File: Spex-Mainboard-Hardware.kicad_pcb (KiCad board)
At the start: 4 copper layers, 100 x 80 mm, 134 parts, among them K1 G5LE_1A4_DC3, K2 G5LE_1A4_DC3, P1 USB_OTG, P10 CONN_01X02, P11 CONN_01X02, P12 CONN_01X02, P13 CONN_01X02, P2 SWD Header, P3 CONN_01X04, P4 CONN_01X04, P5 CONN_01X04, P6 CONN_01X04, P7 CONN_01X02, P8 CONN_01X02, P9 CONN_01X02, Q1 2N7002K, Q101 MOS_N_numbered, Q104 MOS_N_numbered, Q105 Si3407DV, Q106 Q_PNP_BEC, Q2 2N7002K, Q3 BSS215PH6327, Q4 Si5468DC, Q5 Si5468DC, Q6 Si5468DC, SW1 SW_PUSH, U1 MKL04Z32VLC4, U10 LM4030, U105 TPS563200, U108 TPS563200, U11 MCP2551-I/SN, U12 ST1480ABDR, U13 SCHA4B0419, U14 AT45DB641E, U2 NUP2201MR6, U3 MK20DX256VLH7, U4 NUP2201MR6, U5 NUP2201MR6, U6 MMQA6V2T1G, U7 MCP9808T, U8 BME280, U9 LSM9DS1, Y1 Crystal

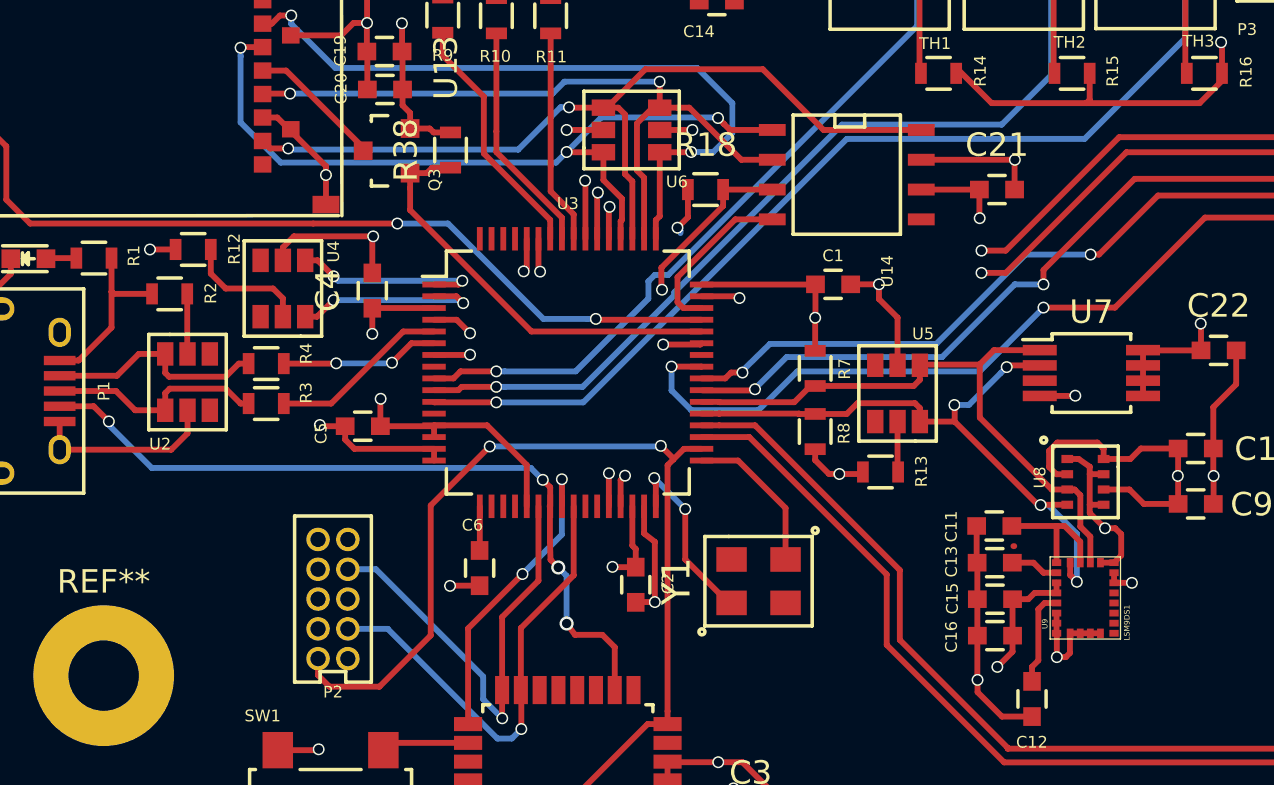
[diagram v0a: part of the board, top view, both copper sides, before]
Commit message: updated BOM, fixed footprints
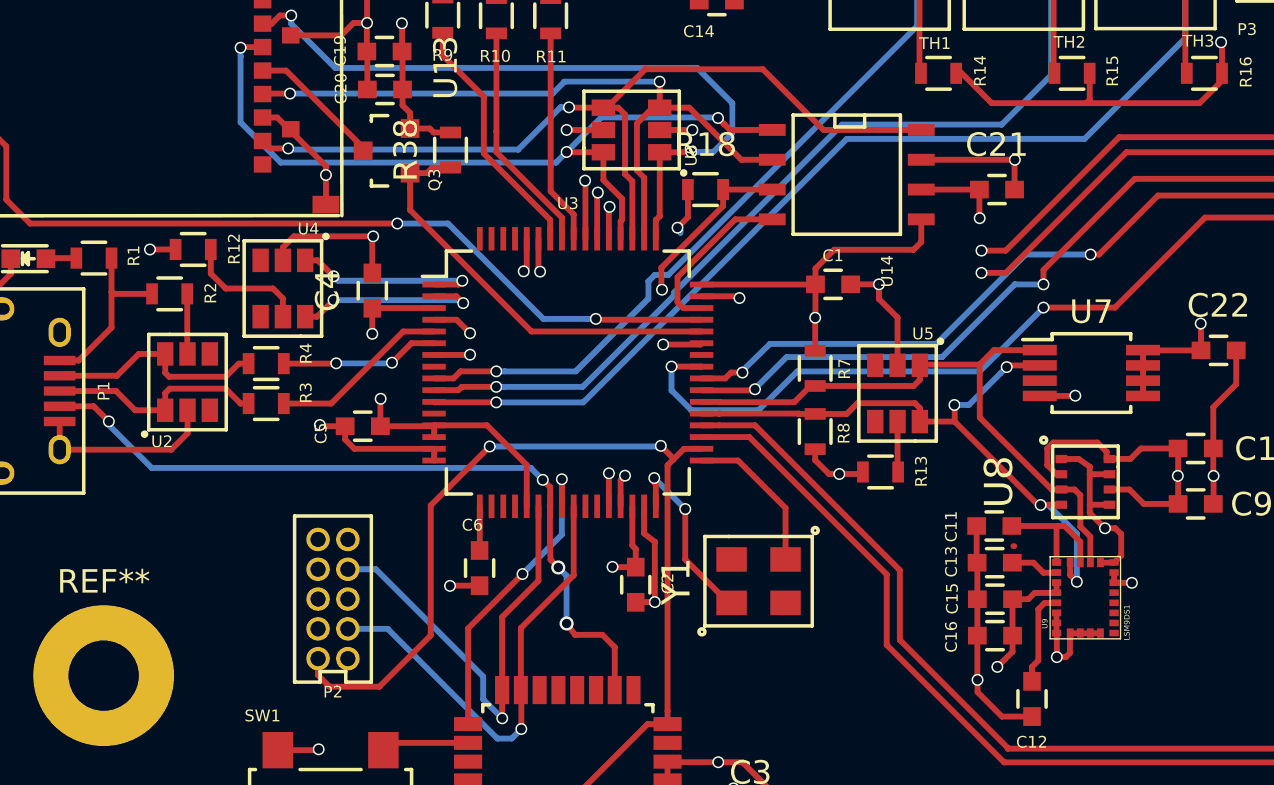
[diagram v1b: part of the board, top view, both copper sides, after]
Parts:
- moved U9 1.95 mm to (131.8, 81.7)
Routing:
- net +3V3: track 131.4 -> 137.6 mm

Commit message: updated PCB
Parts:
- moved REF** 0.19 mm to (90.1, 84.8)
- moved REF** 0.14 mm to (90.0, 125.9)
- moved U13 0.10 mm to (100.0, 65.4)
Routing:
- net (no net): track 2.73 -> 0.07 mm
- net VBatt: track 107.1 -> 107.7 mm
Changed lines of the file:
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@@
     (links 362)
     (no_connects 6)
-    (area 83.744999 50.734999 183.895001 130.885001)
+    (area 79.80956 50.49938 188.775001 131.514133)
     (thickness 1.6)
     (drawings 8)
-    (tracks 1408)
+    (tracks 1406)
     (zones 0)
     (modules 134)
@@
     (0 F.Cu signal)
     (1 In1.Cu power hide)
-    (2 In2.Cu power hide)
+    (2 In2.Cu power)
     (31 B.Cu mixed hide)
     (32 B.Adhes user)
@@
     (user_trace_width 2)
     (trace_clearance 0.15)
-    (zone_clearance 0.1)
+    (zone_clearance 0.508)
     (zone_45_only yes)
     (trace_min 0.2)
@@
     (visible_elements 7FFCFFFF)
     (pcbplotparams
-      (layerselection 0x3ffff_80000007)
+      (layerselection 0x310f0_80000007)
       (usegerberextensions false)
       (excludeedgelayer true)
@@
   )
   (module SPEX_Parts:SCH4B0419 (layer F.Cu)
-    (at 99.8982 65.3796 90)
+    (at 99.99472 65.38976 90)
     (fp_text reference U13 (at 6.2865 4.68884 90) (layer F.SilkS)
       (effects (font (size 1 1) (thickness 0.15)))
@@
   )
   (module Mounting_Holes:MountingHole_3mm_Pad (layer F.Cu)
-    (at 90 126)
+    (at 90.018 125.866)
     (descr "Mounting Hole 3mm")
     (tags "mounting hole 3mm")
@@
   )
   (module Mounting_Holes:MountingHole_3mm_Pad (layer F.Cu)
-    (at 90 85)
+    (at 90.054 84.813)
     (descr "Mounting Hole 3mm")
     (tags "mounting hole 3mm")
@@
     (fp_circle (center 0 0) (end 3 0) (layer Cmts.User) (width 0.15))
     (fp_circle (center 0 0) (end 3.25 0) (layer F.CrtYd) (width 0.05))
-    (pad 1 thru_hole circle (at 0 0) (size 6 6) (drill 3) (layers *.Cu *.Mask F.SilkS))
+    (pad 1 thru_hole circle (at 0.014 0.02) (size 6 6) (drill 3) (layers *.Cu *.Mask F.SilkS))
   )
   (module SPEX_Parts:LGA-8 (layer F.Cu)
@@
   (segment (start 128.766 79.48168) (end 128.8034 79.48168) (width 0.25) (layer F.Cu) (net 0))
   (segment (start 162.5346 78.994) (end 162.56 78.9686) (width 0.25) (layer In2.Cu) (net 0))
-  (segment (start 105.2322 51.7144) (end 105.2322 51.7398) (width 0.25) (layer B.Cu) (net 0))
-  (segment (start 179.6034 79.7372) (end 180.7034 79.7372) (width 0.25) (layer In1.Cu) (net 0))
-  (segment (start 180.7034 79.7372) (end 181.789 80.8228) (width 0.25) (layer In1.Cu) (net 0))
   (segment (start 120.3318 68.326) (end 120.3318 67.6536) (width 0.25) (layer F.Cu) (net 1))
   (segment (start 124.841 66.5226) (end 124.841 65.5574) (width 0.25) (layer F.Cu) (net 1))
@@
   (segment (start 142.2461 55.10682) (end 142.2461 53.4543) (width 0.25) (layer F.Cu) (net 28))
   (segment (start 141.83614 55.51678) (end 142.2461 55.10682) (width 0.25) (layer F.Cu) (net 28))
-  (segment (start 105.283 68.1736) (end 105.283 63.611511) (width 0.25) (layer In1.Cu) (net 28))
+  (segment (start 105.283 68.1736) (end 105.283 63.215127) (width 0.25) (layer In1.Cu) (net 28))
   (segment (start 142.2461 55.06618) (end 142.2461 53.4543) (width 0.25) (layer In1.Cu) (net 28))
   (segment (start 140.55344 56.75884) (end 142.2461 55.06618) (width 0.25) (layer In1.Cu) (net 28))
-  (segment (start 112.131383 56.75884) (end 140.55344 56.75884) (width 0.25) (layer In1.Cu) (net 28))
-  (segment (start 105.283 63.611511) (end 112.131383 56.75884) (width 0.25) (layer In1.Cu) (net 28))
+  (segment (start 111.735247 56.75884) (end 140.55344 56.75884) (width 0.25) (layer In1.Cu) (net 28))
+  (segment (start 105.283 63.215127) (end 111.735247 56.75884) (width 0.25) (layer In1.Cu) (net 28))
   (segment (start 105.283 68.1736) (end 99.9871 68.1736) (width 0.25) (layer B.Cu) (net 28))
   (segment (start 99.1173 67.3038) (end 99.7966 67.9831) (width 0.25) (layer F.Cu) (net 28))
@@
   (segment (start 144.2461 55.3852) (end 144.2461 53.4543) (width 0.25) (layer In1.Cu) (net 29))
   (segment (start 142.29842 57.33288) (end 144.2461 55.3852) (width 0.25) (layer In1.Cu) (net 29))
-  (segment (start 112.36198 57.33288) (end 142.29842 57.33288) (width 0.25) (layer In1.Cu) (net 29))
-  (segment (start 105.95864 63.73622) (end 112.36198 57.33288) (width 0.25) (layer In1.Cu) (net 29))
-  (segment (start 105.95864 68.53682) (end 105.95864 63.73622) (width 0.25) (layer In1.Cu) (net 29))
+  (segment (start 111.9505 57.33288) (end 142.29842 57.33288) (width 0.25) (layer In1.Cu) (net 29))
+  (segment (start 105.95864 63.32474) (end 111.9505 57.33288) (width 0.25) (layer In1.Cu) (net 29))
+  (segment (start 105.95864 68.53682) (end 105.95864 63.32474) (width 0.25) (layer In1.Cu) (net 29))
   (segment (start 105.36936 69.1261) (end 105.95864 68.53682) (width 0.25) (layer In1.Cu) (net 29))
   (segment (start 144.4752 58.74442) (end 144.4752 55.6641) (width 0.25) (layer F.Cu) (net 29))
@@
   (segment (start 146.4056 66.3194) (end 142.1638 70.5612) (width 0.25) (layer F.Cu) (net 47))
   (segment (start 141.80459 70.5612) (end 142.1638 70.5612) (width 0.25) (layer In1.Cu) (net 47))
-  (segment (start 111.5314 76.01859) (end 116.982401 70.567589) (width 0.25) (layer In1.Cu) (net 47))
+  (segment (start 111.5314 75.72649) (end 116.690301 70.567589) (width 0.25) (layer In1.Cu) (net 47))
   (segment (start 141.732 70.567589) (end 141.738389 70.5612) (width 0.25) (layer In1.Cu) (net 47))
   (segment (start 141.738389 70.5612) (end 141.80459 70.5612) (width 0.25) (layer In1.Cu) (net 47))
-  (segment (start 116.982401 70.567589) (end 141.732 70.567589) (width 0.25) (layer In1.Cu) (net 47))
-  (segment (start 111.5314 76.3778) (end 111.5314 76.01859) (width 0.25) (layer In1.Cu) (net 47))
+  (segment (start 116.690301 70.567589) (end 141.732 70.567589) (width 0.25) (layer In1.Cu) (net 47))
+  (segment (start 111.5314 76.3778) (end 111.5314 75.72649) (width 0.25) (layer In1.Cu) (net 47))
   (segment (start 168.111911 59.602753) (end 167.680111 59.602753) (width 0.25) (layer F.Cu) (net 47))
   (via (at 142.1638 70.5612) (size 0.508) (drill 0.381) (layers F.Cu B.Cu) (net 47))
@@
   (segment (start 112.7252 63.4746) (end 113.0288 63.7782) (width 0.25) (layer F.Cu) (net 53))
   (segment (start 113.0288 63.7782) (end 113.0288 66.3852) (width 0.25) (layer F.Cu) (net 53))
+  (segment (start 109.87024 60.36056) (end 109.616241 60.614559) (width 0.25) (layer B.Cu) (net 54))
+  (segment (start 109.616241 60.614559) (end 109.616241 60.636349) (width 0.25) (layer B.Cu) (net 54))
+  (segment (start 109.616241 60.636349) (end 107.66699 62.5856) (width 0.25) (layer B.Cu) (net 54))
+  (segment (start 111.2966 60.7974) (end 110.30708 60.7974) (width 0.25) (layer F.Cu) (net 54))
+  (segment (start 110.30708 60.7974) (end 109.87024 60.36056) (width 0.25) (layer F.Cu) (net 54))
   (segment (start 124.841 61.7474) (end 120.6754 61.7474) (width 0.25) (layer F.Cu) (net 54))
   (segment (start 120.6754 61.7474) (end 118.088998 59.160998) (width 0.25) (layer F.Cu) (net 54))
@@
   (segment (start 97.917 62.5856) (end 97.8662 62.5348) (width 0.25) (layer B.Cu) (net 54))
   (via (at 97.8662 62.5348) (size 0.508) (drill 0.381) (layers F.Cu B.Cu) (net 54))
-  (segment (start 109.47039 60.7822) (end 107.66699 62.5856) (width 0.25) (layer B.Cu) (net 54))
-  (segment (start 109.8296 60.7822) (end 109.47039 60.7822) (width 0.25) (layer B.Cu) (net 54))
-  (segment (start 111.2966 60.7974) (end 109.8448 60.7974) (width 0.25) (layer F.Cu) (net 54))
-  (via (at 109.8296 60.7822) (size 0.508) (drill 0.381) (layers F.Cu B.Cu) (net 54))
-  (segment (start 109.8448 60.7974) (end 109.8296 60.7822) (width 0.25) (layer F.Cu) (net 54))
+  (via (at 109.87024 60.36056) (size 0.508) (drill 0.381) (layers F.Cu B.Cu) (net 54))
   (segment (start 112.2172 61.1378) (end 112.2172 61.087) (width 0.25) (layer F.Cu) (net 54))
   (segment (start 112.2172 61.1378) (end 112.2172 63.627) (width 0.25) (layer F.Cu) (net 54))
@@
   (segment (start 147.5 99.5) (end 147.5 100.5) (width 1) (layer In2.Cu) (net 77))
   (segment (start 147.5 100.5) (end 147.5 101.5) (width 1) (layer In2.Cu) (net 77))
-  (segment (start 157.4094 104.6126) (end 157.4094 104.552) (width 0.25) (layer In2.Cu) (net 77))
-  (segment (start 157.4094 104.552) (end 153.3574 100.5) (width 1) (layer In2.Cu) (net 77))
-  (segment (start 153.3574 100.5) (end 147.5 100.5) (width 1) (layer In2.Cu) (net 77))
+  (segment (start 157.4094 104.6126) (end 157.4094 103.54616) (width 0.25) (layer In2.Cu) (net 77))
+  (segment (start 157.4094 103.54616) (end 154.36324 100.5) (width 1) (layer In2.Cu) (net 77))
+  (segment (start 154.36324 100.5) (end 147.5 100.5) (width 1) (layer In2.Cu) (net 77))
   (segment (start 143.5 98.5) (end 143.5 100.8) (width 2) (layer F.Cu) (net 77))
   (segment (start 147.5 100.5) (end 143.8 100.5) (width 2) (layer F.Cu) (net 77))
@@
   )
   (zone (net 2) (net_name GND) (layer In1.Cu) (hatch edge 0.508)
-    (connect_pads (clearance 0.508))
+    (connect_pads (clearance 0.45))
     (min_thickness 0.254)
     (fill yes (arc_segments 16) (thermal_gap 1.016) (thermal_bridge_width 0.508))

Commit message: rev 2 of hab board in progress
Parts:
- removed D110: DIODE, Diodes_SMD:Diode-SMA_Standard
- removed D5, D6: FM5819-W, Diodes_SMD:SMA_Standard
- removed K1, K2: G5LE_1A4_DC3, SPEX_Parts:G5LE-1A4-DC3
- removed P2: SWD Header, SPEX_Parts:SWD-10
- removed Q1, Q2: 2N7002K, TO_SOT_Packages_SMD:SOT-23
- removed R29, R34: 10K, Resistors_SMD:R_0603
- removed REF** (x3): MountingHole_3mm_Pad, Mounting_Holes:MountingHole_3mm_Pad
- added SW2: SW_PUSH, Buttons_Switches_SMD:SW_SPST_B3S-1000, F.Cu at (48.7, 103.7)
- C10, C9: value C -> 100nF
- C17, C18, C21, C22: value C -> 1uF
- D109: footprint Transistors_SMD:sc70 -> TO_SOT_Packages_SMD:SC-70
- Q101, Q104, Q106: footprint Housings_SOT-23_SOT-143_TSOT-6:SOT-23 -> TO_SOT_Packages_SMD:SOT-23
- R17: value R -> 240
- R28: value R -> 4.7K
- U1: value MKL04Z32VLC4 -> MKL02Z32VFG4; footprint Housings_QFP:LQFP-32_7x7mm_Pitch0.8mm -> SPEX_Parts:QFN-16-1EP_3x3mm_Pitch0.5mm
- U105, U108: footprint Housings_SOT-23_SOT-143_TSOT-6:SOT-23-6 -> TO_SOT_Packages_SMD:SOT-23-6
- moved P13 181.9 mm to (247.7, 30.0), turned to 0 degrees
- moved R147 153.0 mm to (251.4, 49.2), turned to 0 degrees
- moved R141 151.2 mm to (246.2, 55.9)
- moved P11 150.9 mm to (173.0, -32.9), turned to 0 degrees
- moved C118 147.6 mm to (246.5, 49.6), turned to 0 degrees
- moved U108 144.6 mm to (239.5, 50.2), turned to 0 degrees
- moved R140 144.6 mm to (238.2, 57.1), turned to 0 degrees
- moved P9 144.3 mm to (111.9, -26.3), turned to 0 degrees
- moved C121 142.2 mm to (242.9, 61.8), turned to 0 degrees
- moved P8 142.2 mm to (95.4, -26.3), turned to 0 degrees
- moved P12 142.0 mm to (182.2, -32.7), turned to 0 degrees
- moved Q104 140.5 mm to (228.2, 49.5)
- moved R145 137.9 mm to (238.2, 63.0), turned to 0 degrees
- moved P6 130.2 mm to (88.7, 152.2), turned to 180 degrees
- moved C122 128.6 mm to (233.5, 57.5), turned to 0 degrees
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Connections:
- U1 pad 1: Net-(U1-Pad1) -> +3V3
- U1 pad 10: /PTA6 -> /PTB2
- U1 pad 13: Net-(U1-Pad13) -> RESET_b
- U1 pad 15: /PTA7 -> Net-(U1-Pad15)
- U1 pad 16: /PTB0 -> Net-(U1-Pad16)
- U1 pad 2: Net-(U1-Pad2) -> GND
- U1 pad 3: +3V3 -> Net-(U1-Pad3)
- U1 pad 4: +3V3 -> RESET_b
- U1 pad 5: GND -> Net-(U1-Pad5)
- U1 pad 6: GND -> /PTA6
- U1 pad 7: Net-(U1-Pad7) -> /PTA7
- U1 pad 8: RESET_b -> /PTB0
- U1 pad 9: Net-(U1-Pad9) -> /PTB1
- U3 pad 51: SPI0_MISO -> SPI0_MOSI
- U3 pad 52: SPI0_MOSI -> SPI0_MISO
- U3 pad 64: Net-(U3-Pad64) -> /Toggle
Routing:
- net GND: track 301.5 -> 76.1 mm, vias 49 -> 37
- net Vbus: track 144.4 -> 0.00 mm, vias 24 -> 0
- net VBatt: track 107.7 -> 0.00 mm, vias 14 -> 0
- net +5V: track 99.3 -> 0.00 mm, vias 12 -> 0
- net Vbus_MOS_CTRL: track 78.3 -> 0.00 mm, vias 2 -> 0
- net 5V_MOS_CTRL: track 72.1 -> 0.00 mm, vias 2 -> 0
- net 3.3V_MOS_CTRL: track 67.6 -> 0.00 mm, vias 2 -> 0
- net I2C1_SCL: track 64.1 -> 0.00 mm, vias 2 -> 0
- net Relay1_ctrl: track 62.5 -> 0.00 mm, vias 2 -> 0
- net CAN0_RX: track 63.4 -> 2.24 mm, vias 2 -> 0
- net I2C1_SDA: track 60.7 -> 0.00 mm, vias 2 -> 0
- net CAN0_TX: track 66.7 -> 7.20 mm, vias 2 -> 0
- net UART2_RX: track 54.3 -> 0.00 mm, vias 2 -> 0
- net UART2_TX: track 53.3 -> 0.00 mm, vias 2 -> 0
- net /Data_Input_Output/User_Out: track 50.3 -> 0.00 mm
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- removed copper zone on F.Cu, net +3V3
- removed copper zone on F.Cu, net +5V
- removed copper zone on F.Cu, net /Data_Input_Output/3.3V_MOS_OUT
- removed copper zone on F.Cu, net /Data_Input_Output/5V_MOS_OUT
- removed copper zone on F.Cu, net /Data_Input_Output/Vbus_MOS_OUT
- removed copper zone on B.Cu, net /Power Distribution/VBus
- removed copper zone on F.Cu, net /Power Distribution/VBus
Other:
- board size 100 x 80 mm -> 100 x 100 mm
- net class 6mil added: clearance 0.2032, trace_width 0.1524, via_dia 0.6, via_drill 0.4
- net class Default: clearance 0.15 -> 0.2032; trace_width 0.25 -> 0.254; via_dia 0.508 -> 0.6; via_drill 0.381 -> 0.4
- net class Power removed
- rule pad_to_mask_clearance: 0.2 -> 0
- rule trace_clearance: 0.15 -> 0.2032
- rule trace_min: 0.2 -> 0.1524
- board text removed: "POWER IN (VBAT)"
- board text removed: "RIT SPEX HAB 2 MAINBOARD DESIGNERS: MATTHEW GLAZER CHRIS CULPEPPER"
- board text removed: "Revision: 1 Design Date: 4/16"
- board text removed: "TIGRIS AD ASTRA"

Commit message: routing power, digital portion mostly complete
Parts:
- added D110: DIODE, Diodes_SMD:SMA_Standard, F.Cu at (48.4, 90.5)
- moved P13 234.3 mm to (20.8, 88.8), turned to 90 degrees
- moved R149 161.5 mm to (51.1, 98.2)
- moved R152 158.2 mm to (46.3, 94.2), turned to 90 degrees
- moved P9 146.6 mm to (104.2, 120.1), turned to 270 degrees
- moved C119 146.4 mm to (58.8, 92.1), turned to 270 degrees
- moved Q106 146.0 mm to (51.8, 94.3), turned to 90 degrees
- moved R150 145.7 mm to (53.7, 89.7), turned to 90 degrees
- moved R146 143.6 mm to (56.3, 95.9), turned to 270 degrees
- moved C14 142.5 mm to (81.0, 43.5)
- moved R14 142.5 mm to (52.8, 44.9)
- moved R15 142.5 mm to (59.9, 44.9)
- moved R16 142.5 mm to (67.1, 44.0)
- moved R17 142.5 mm to (80.8, 33.9)
- moved TH1 142.5 mm to (53.0, 38.5)
- moved TH2 142.5 mm to (59.3, 38.3)
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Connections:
- U10 pad 2: GND -> Net-(U10-Pad2)
- U10 pad 5: GND -> Net-(U10-Pad2)
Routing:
- net Net-(C119-Pad1): track 0.00 -> 12.6 mm
- net Net-(C119-Pad2): track 0.00 -> 9.55 mm
- net GND: track 76.1 -> 83.0 mm, vias 37 -> 39
- net Net-(D108-Pad1): track 0.00 -> 6.64 mm
- net Net-(D110-Pad2): track 0.00 -> 6.38 mm
- net Net-(C123-Pad1): track 0.00 -> 2.75 mm
- net Net-(D108-Pad2): track 0.00 -> 2.03 mm
- added copper zone on F.Cu, net VBatt

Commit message: continued work on power electronics
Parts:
- moved L103 23.4 mm to (242.3, 41.9), turned to 180 degrees
- moved C120 19.1 mm to (62.9, 94.4)
- moved R151 17.5 mm to (63.6, 89.9), turned to 90 degrees
- moved D109 17.1 mm to (66.5, 89.9), turned to 270 degrees
- moved Q105 12.7 mm to (59.5, 96.0)
- moved R146 10.9 mm to (56.7, 85.0), turned to 90 degrees
- moved C118 10.8 mm to (235.7, 50.3), turned to 90 degrees
- moved R148 7.07 mm to (61.5, 89.8), turned to 90 degrees
- moved D106 3.54 mm to (56.7, 88.7), turned to 90 degrees
- moved C119 3.33 mm to (59.2, 88.8), turned to 90 degrees
- turned U108 to 270 degrees
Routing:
- net Net-(C119-Pad2): track 9.55 -> 25.8 mm, vias 0 -> 2
- net Net-(C119-Pad1): track 12.6 -> 17.8 mm
- net Net-(Q105-Pad3): track 0.00 -> 4.56 mm
- net Net-(C120-Pad2): track 0.00 -> 4.52 mm
- net GND: track 83.0 -> 81.4 mm, vias 39 -> 41

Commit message: the routing never ends
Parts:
- removed P10, P11, P12: CONN_01X02, SPEX_Parts:ultraFitCONN_2
- added REF**: MountingHole_3.2mm_M3_Pad, Mounting_Holes:MountingHole_3.2mm_M3_Pad, F.Cu at (21.4, 160.1)
- added REF**: MountingHole_3.2mm_M3_Pad, Mounting_Holes:MountingHole_3.2mm_M3_Pad, F.Cu at (21.1, 86.0)
- added REF**: MountingHole_3.2mm_M3_Pad, Mounting_Holes:MountingHole_3.2mm_M3_Pad, F.Cu at (111.0, 84.8)
- added REF**: MountingHole_3.2mm_M3_Pad, Mounting_Holes:MountingHole_3.2mm_M3_Pad, F.Cu at (106.4, 158.7)
- moved L103 188.6 mm to (60.0, 90.3), turned to 270 degrees
- moved R147 184.7 mm to (71.0, 89.2)
- moved C121 177.7 mm to (67.5, 90.3)
- moved U108 177.5 mm to (67.3, 93.1), turned to 0 degrees
- moved R108 176.1 mm to (76.6, 105.6), turned to 270 degrees
- moved C118 174.3 mm to (67.7, 96.8), turned to 180 degrees
- moved R140 172.1 mm to (70.2, 94.0), turned to 270 degrees
- moved R126 171.1 mm to (72.6, 104.2), turned to 180 degrees
- moved R145 169.6 mm to (71.0, 91.3), turned to 180 degrees
- moved C105 169.0 mm to (78.2, 101.6), turned to 270 degrees
- moved C122 168.9 mm to (67.3, 87.4)
- moved C109 167.1 mm to (75.9, 101.4), turned to 270 degrees
- moved L102 164.7 mm to (75.8, 96.9), turned to 180 degrees
- moved C114 164.7 mm to (69.6, 101.8), turned to 90 degrees
- moved R109 164.3 mm to (74.8, 105.6), turned to 90 degrees
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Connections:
- U4 pad 1: I2C1_SDA -> I2C1_SCL
- U4 pad 6: I2C1_SCL -> I2C1_SDA
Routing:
- net UART2_TX: track 0.00 -> 62.7 mm, vias 0 -> 2
- net UART2_RX: track 0.00 -> 60.9 mm, vias 0 -> 2
- net CAN0_RX: track 2.24 -> 51.0 mm, vias 0 -> 2
- net CAN0_TX: track 7.20 -> 53.9 mm, vias 0 -> 2
- net UART0_RX: track 0.00 -> 40.9 mm, vias 0 -> 2
- net /Toggle: track 0.00 -> 39.5 mm, vias 0 -> 2
- net RX/TX_CTRL: track 0.00 -> 37.8 mm, vias 0 -> 2
- net UART0_TX: track 0.00 -> 37.7 mm, vias 0 -> 2
- net Vbus: track 0.00 -> 30.4 mm
- net GND: track 81.4 -> 103.2 mm, vias 41 -> 53
- net +3V3: track 87.3 -> 102.9 mm, vias 16 -> 19
- net +5V: track 0.00 -> 15.1 mm, vias 0 -> 2
- net Net-(C121-Pad1): track 0.00 -> 12.0 mm
- net I2C1_SCL: track 0.00 -> 10.7 mm
- net I2C1_SDA: track 0.00 -> 10.2 mm
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- added copper zone on F.Cu, net +3V3
- added copper zone on F.Cu, net +5V
- added copper zone on F.Cu, net Vbus
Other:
- board size 100 x 100 mm -> 100 x 84.7 mm
